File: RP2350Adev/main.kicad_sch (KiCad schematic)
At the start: 0 parts

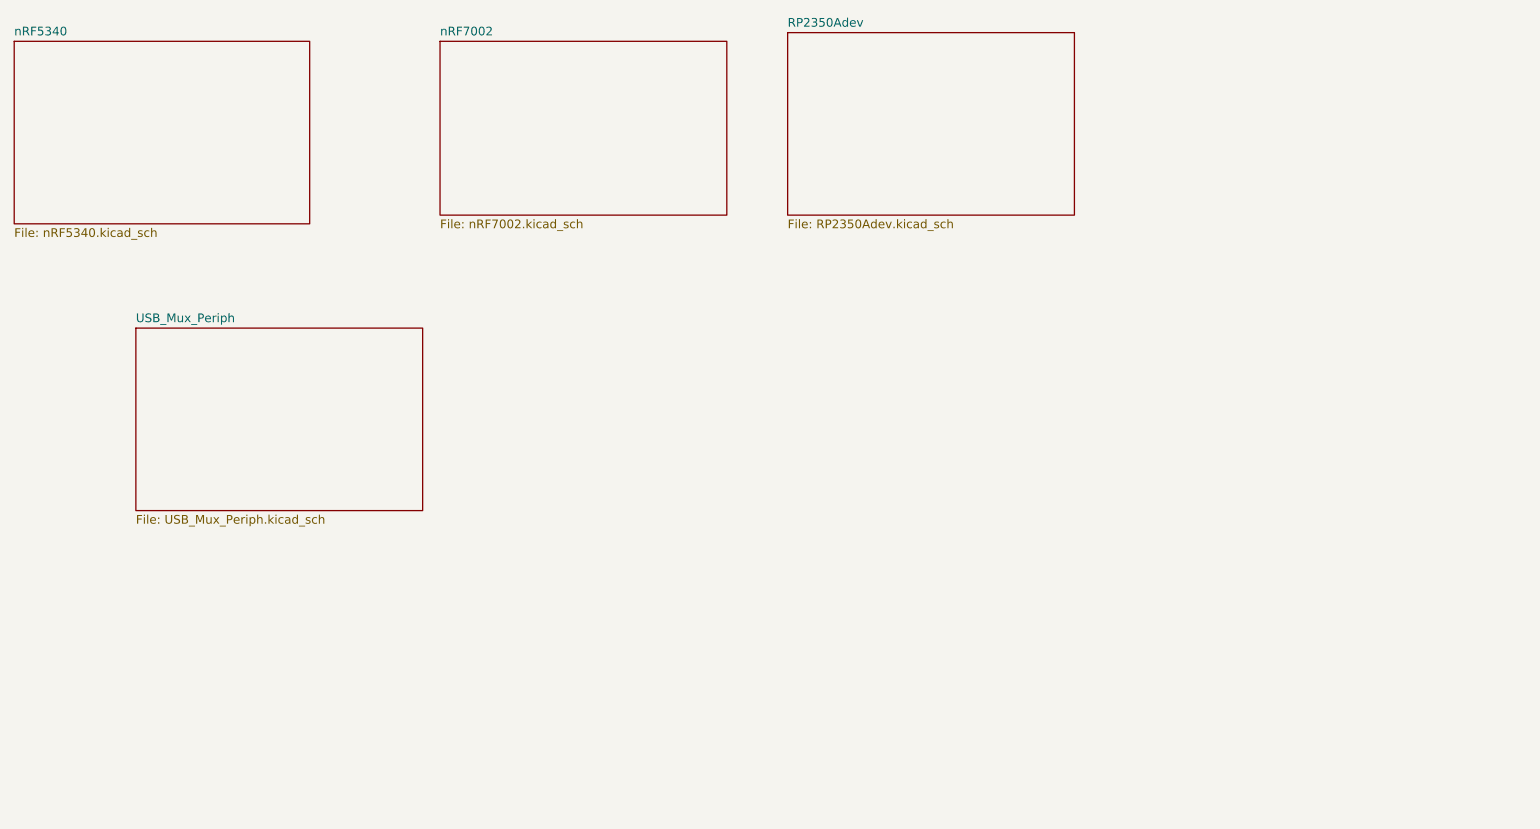
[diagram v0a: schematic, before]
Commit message: Combine subsheets
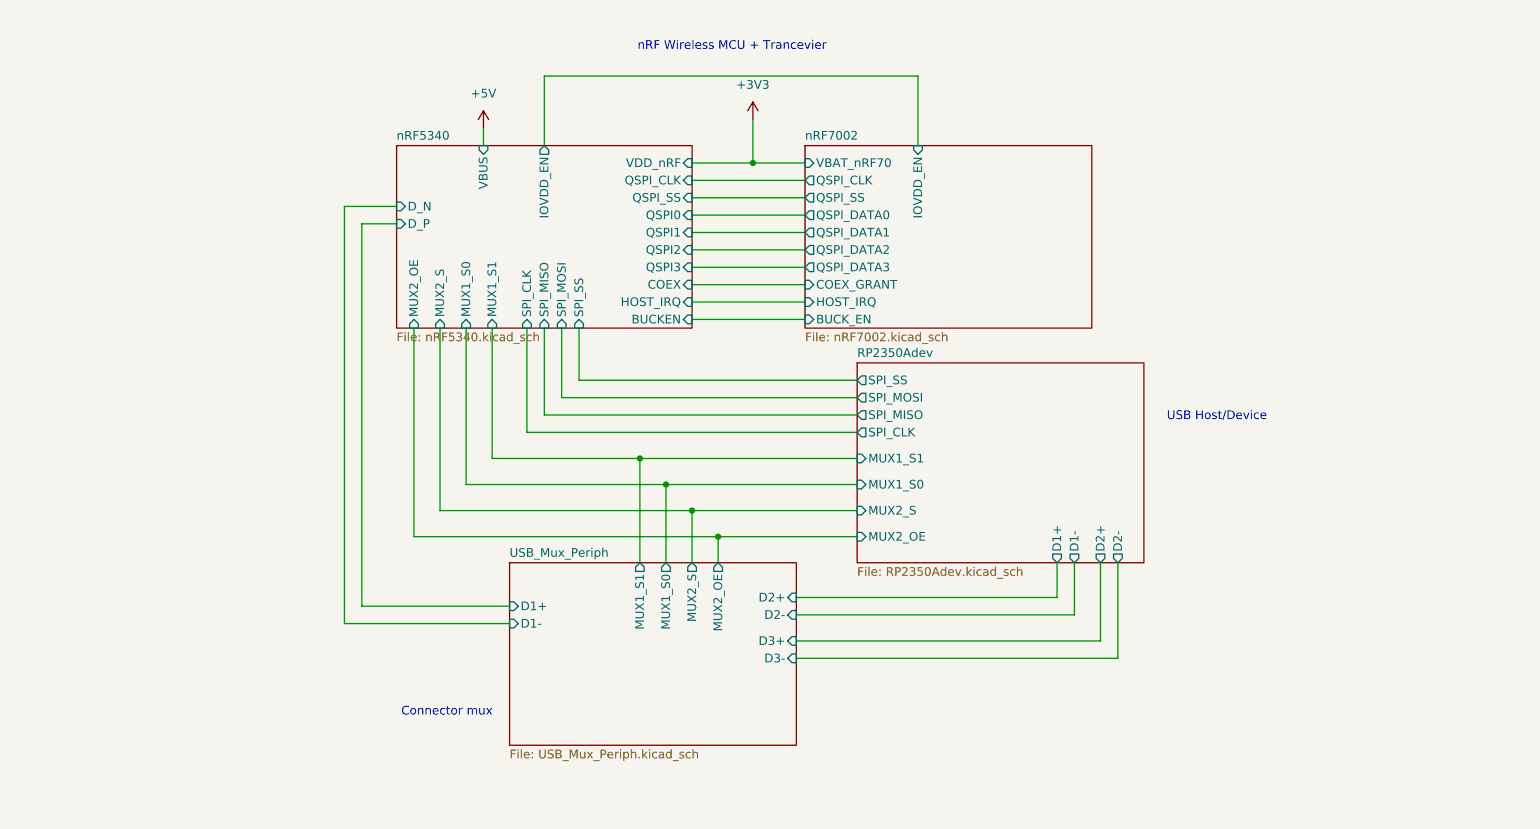
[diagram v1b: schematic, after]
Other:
- sheet RP2350Adev ports: added D1+, D1-, D2+, D2-, MUX1_S0, MUX1_S1, MUX2_OE, MUX2_S, SPI_CLK, SPI_MISO, SPI_MOSI, SPI_SS; removed none
- sheet USB_Mux_Periph ports: added D1+, D1-, D2+, D2-, D3+, D3-, MUX1_S0, MUX1_S1, MUX2_OE, MUX2_S; removed none
- sheet nRF5340 ports: added BUCKEN, COEX, D_N, D_P, HOST_IRQ, IOVDD_EN, MUX1_S0, MUX1_S1, MUX2_OE, MUX2_S, QSPI0, QSPI1, QSPI2, QSPI3, QSPI_CLK, QSPI_SS, SPI_CLK, SPI_MISO, SPI_MOSI, SPI_SS, VBUS, VDD_nRF; removed none
- sheet nRF7002 ports: added BUCK_EN, COEX_GRANT, HOST_IRQ, IOVDD_EN, QSPI_CLK, QSPI_DATA0, QSPI_DATA1, QSPI_DATA2, QSPI_DATA3, QSPI_SS, VBAT_nRF70; removed none
- note added: "Connector mux"
- note added: "USB Host/Device"
- note added: "nRF Wireless MCU + Trancevier"
- title: (none) -> USB Mirror board

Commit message: Combine subcircuits
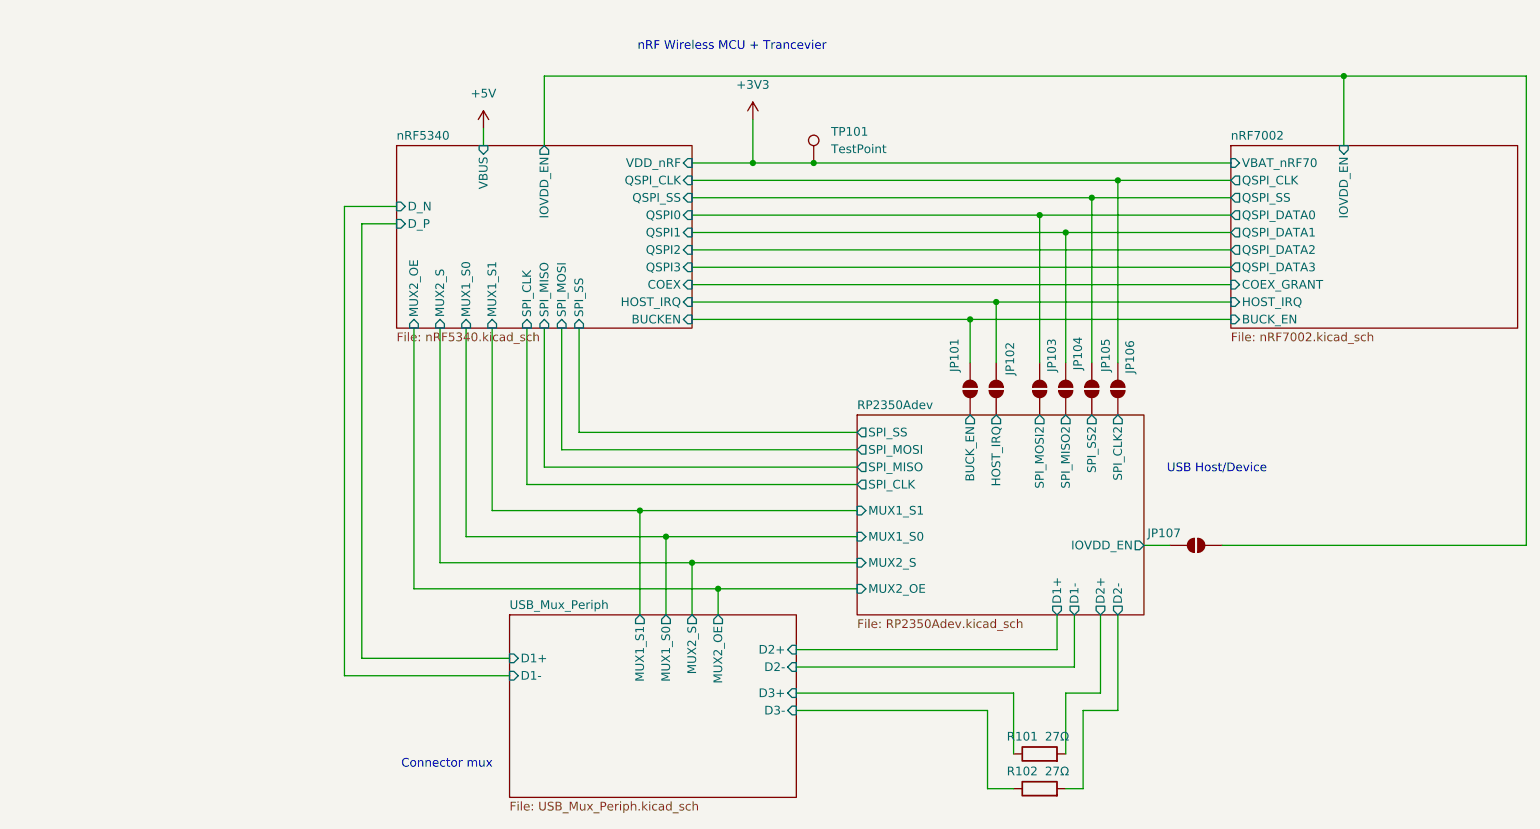
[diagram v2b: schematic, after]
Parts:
- added JP101, JP102, JP103, JP104, JP105, JP106, JP107: SolderJumper_2_Open, Jumper:SolderJumper-2_P1.3mm_Open_RoundedPad1.0x1.5mm, symbol Jumper:SolderJumper_2_Open
- added R101, R102: 27Ω, Resistor_SMD:R_0402_1005Metric, symbol Device:R
- added TP101: TestPoint, TestPoint:TestPoint_Pad_D1.0mm, symbol Connector:TestPoint
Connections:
- net +3V3: now also TP101.1
- net RP2350Adev/D2+: now also R101.2
- net RP2350Adev/D2-: now also R102.2
- net nRF5340/BUCKEN: now also JP101.2 (B)
- net nRF5340/HOST_IRQ: now also JP102.2 (B)
- net nRF5340/IOVDD_EN: now also JP107.1 (A)
- net nRF5340/QSPI0: now also JP103.2 (B)
- net nRF5340/QSPI1: now also JP104.2 (B)
- net nRF5340/QSPI_CLK: now also JP106.2 (B)
- net nRF5340/QSPI_SS: now also JP105.2 (B)
- new net RP2350Adev/BUCK_EN: JP101.1 (A)
- new net RP2350Adev/HOST_IRQ: JP102.1 (A)
- new net RP2350Adev/IOVDD_EN: JP107.2 (B)
- new net RP2350Adev/SPI_CLK2: JP106.1 (A)
- new net RP2350Adev/SPI_MISO2: JP104.1 (A)
- new net RP2350Adev/SPI_MOSI2: JP103.1 (A)
- new net RP2350Adev/SPI_SS2: JP105.1 (A)
- new net USB_Mux_Periph/D3+: R101.1
- new net USB_Mux_Periph/D3-: R102.1
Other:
- sheet RP2350Adev ports: added BUCK_EN, HOST_IRQ, IOVDD_EN, SPI_CLK2, SPI_MISO2, SPI_MOSI2, SPI_SS2; removed none
